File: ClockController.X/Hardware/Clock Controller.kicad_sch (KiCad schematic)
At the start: 0 parts

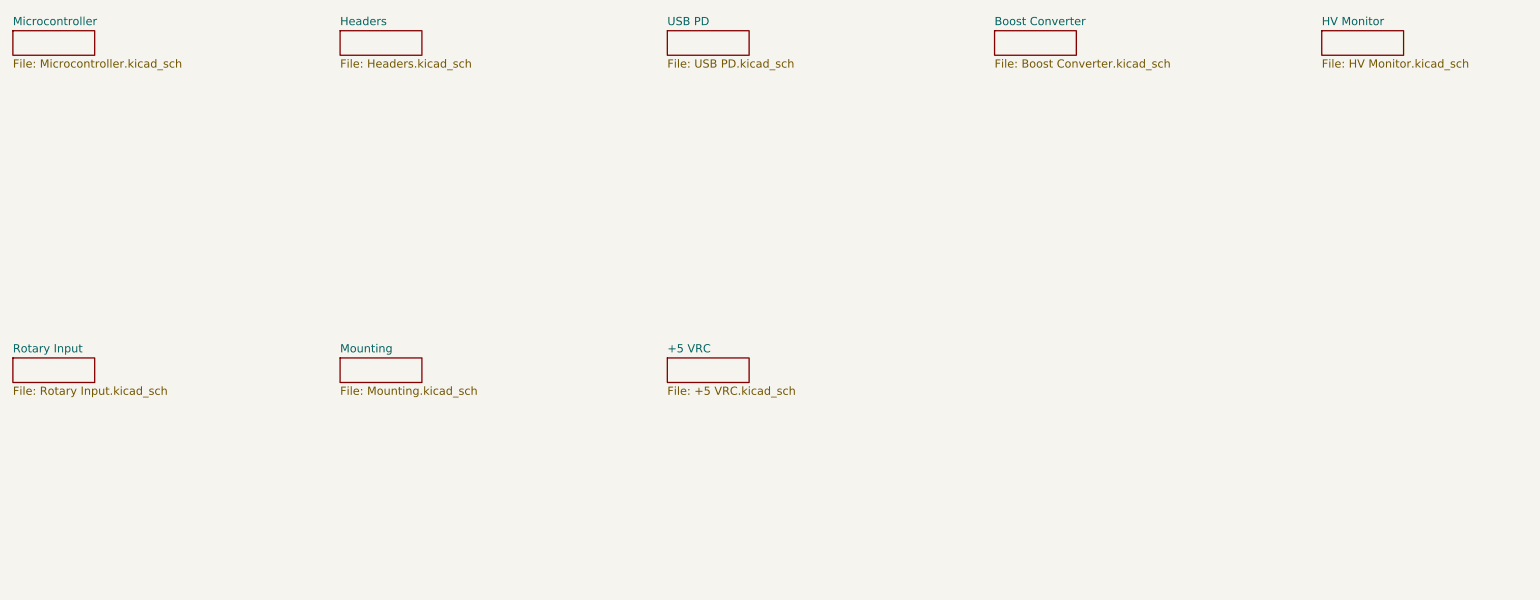
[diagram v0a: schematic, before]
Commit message: Replace the imported objects with native kicad equivalents
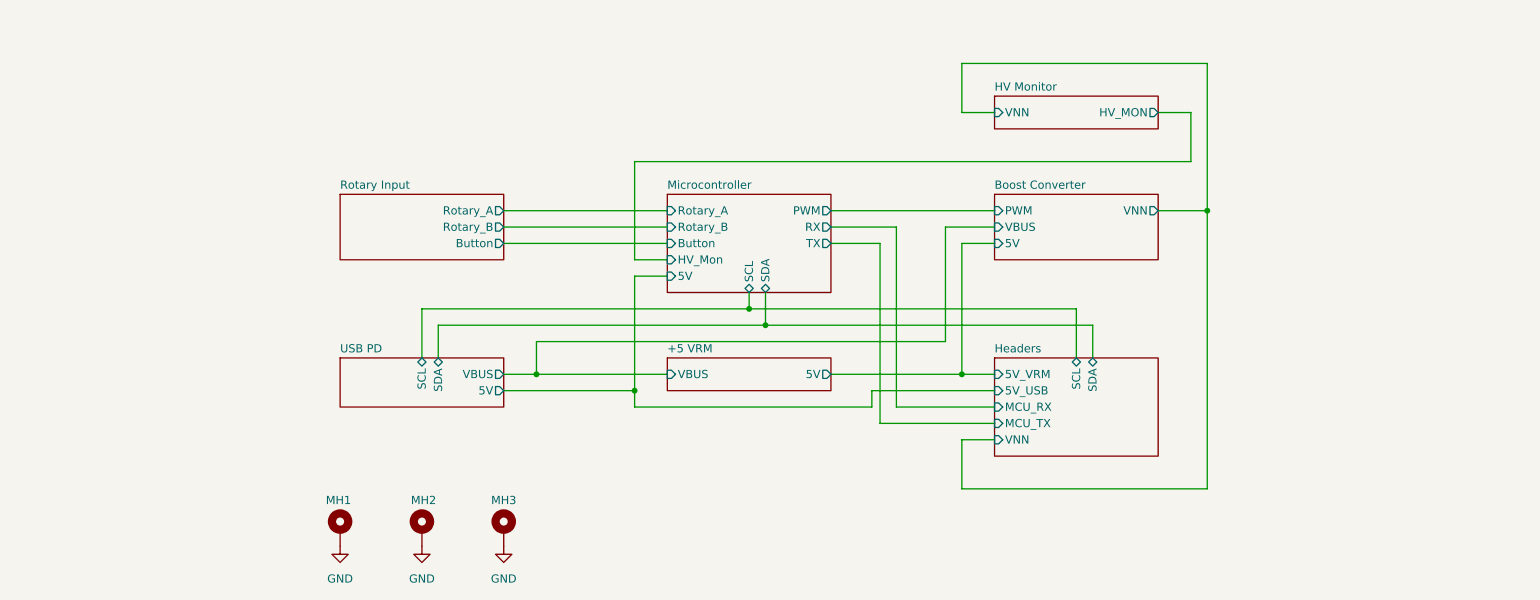
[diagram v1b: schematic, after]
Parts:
- added MH1, MH2, MH3: M2.5_MTGP540H285, MountingHole:MountingHole_2.5mm_Pad, symbol Mechanical:MountingHole_Pad
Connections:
- new net GND: MH1.1, MH2.1, MH3.1
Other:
- sheet +5 VRC renamed +5 VRM
- removed sheet Mounting
- sheet +5 VRM ports: added 5V, VBUS; removed none
- sheet Boost Converter ports: added 5V, PWM, VBUS, VNN; removed none
- sheet HV Monitor ports: added HV_MON, VNN; removed none
- sheet Headers ports: added 5V_USB, 5V_VRM, MCU_RX, MCU_TX, SCL, SDA, VNN; removed none
- sheet Microcontroller ports: added 5V, Button, HV_Mon, PWM, RX, Rotary_A, Rotary_B, SCL, SDA, TX; removed none
- sheet Rotary Input ports: added Button, Rotary_A, Rotary_B; removed none
- sheet USB PD ports: added 5V, SCL, SDA, VBUS; removed none
